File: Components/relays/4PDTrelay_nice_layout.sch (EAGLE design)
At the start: 1 part

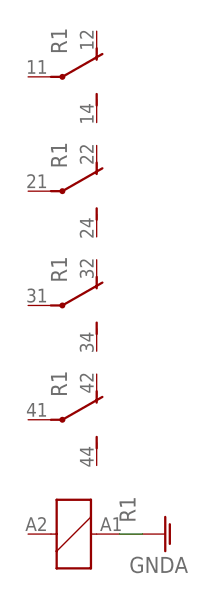
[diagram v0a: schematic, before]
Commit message: Creating re-usable suppressed relay components w/ vertical diodes
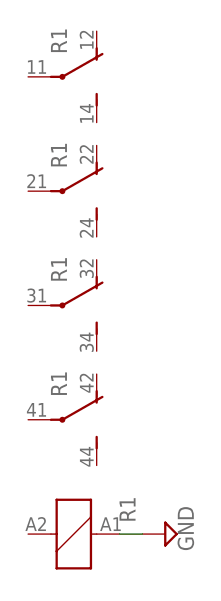
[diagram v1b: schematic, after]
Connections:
- net GNDA renamed GND
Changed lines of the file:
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@@
 <?xml version="1.0" encoding="utf-8"?>
 <!DOCTYPE eagle SYSTEM "eagle.dtd">
-<eagle version="8.2.1">
+<eagle version="8.3.2">
 <drawing>
 <settings>
 <setting alwaysvectorfont="no"/>
+<setting keepoldvectorfont="yes"/>
 <setting verticaltext="up"/>
 </settings>
@@
 <layer number="97" name="Info" color="7" fill="1" visible="yes" active="yes"/>
 <layer number="98" name="Guide" color="6" fill="1" visible="yes" active="yes"/>
+<layer number="99" name="SpiceOrder" color="5" fill="1" visible="yes" active="yes"/>
 </layers>
 <schematic xreflabel="%F%N/%S.%C%R" xrefpart="/%S.%C%R">
@@
 </classes>
 <parts>
-<part name="GND1" library="supply1" deviceset="GNDA" device=""/>
 <part name="R1" library="relay_computer_custom" deviceset="PT5*" device="" technology="71R06"/>
+<part name="SUPPLY1" library="supply2" library_urn="urn:adsk.eagle:library:372" deviceset="GND" device=""/>
 </parts>
 <sheets>
@@
 </plain>
 <instances>
-<instance part="GND1" gate="1" x="73.66" y="17.78" rot="R90"/>
 <instance part="R1" gate="1" x="63.5" y="17.78" rot="MR90"/>
 <instance part="R1" gate="2" x="60.96" y="68.58" rot="MR90"/>
@@
 <instance part="R1" gate="4" x="60.96" y="43.18" rot="MR90"/>
 <instance part="R1" gate="5" x="60.96" y="30.48" rot="MR90"/>
+<instance part="SUPPLY1" gate="GND" x="73.66" y="17.78" rot="R90"/>
 </instances>
 <busses>
 </busses>
 <nets>
-<net name="GNDA" class="0">
+<net name="GND" class="0">
 <segment>
 <pinref part="R1" gate="1" pin="1"/>
-<pinref part="GND1" gate="1" pin="GNDA"/>
 <wire x1="68.58" y1="17.78" x2="71.12" y2="17.78" width="0.1524" layer="91"/>
+<pinref part="SUPPLY1" gate="GND" pin="GND"/>
 </segment>
 </net>
@@
 </schematic>
 </drawing>
+<compatibility>
+<note version="8.2" severity="warning">
+Since Version 8.2, EAGLE supports online libraries. The ids
+of those online libraries will not be understood (or retained)
+with this version.
+</note>
+<note version="8.3" severity="warning">
+Since Version 8.3, EAGLE supports URNs for individual library
+assets (packages, symbols, and devices). The URNs of those assets
+will not be understood (or retained) with this version.
+</note>
+</compatibility>
 </eagle>
